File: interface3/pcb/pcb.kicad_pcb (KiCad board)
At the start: 4 copper layers, 55 x 50 mm, 26 parts, among them J1 Conn_Coaxial, T1 Murata 78602/8JC, U1 DS34LV86T, U2 DS34LV87T

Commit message: some pcb work
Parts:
- added U3: Pico_W, library:RPi_Pico_W_SMD_TH, F.Cu at (60.4, 86.4)
- moved C3 30.6 mm to (43.5, 105.7), turned to 0 degrees
- moved C1 28.6 mm to (43.5, 103.9), turned to 0 degrees
- moved C4 24.0 mm to (31.5, 105.7), turned to 0 degrees
- moved C2 21.5 mm to (31.5, 103.9), turned to 0 degrees
- moved U1 18.6 mm to (38.0, 99.2), turned to -90 degrees
- moved U2 16.7 mm to (26.0, 99.2), turned to -90 degrees
- moved H2 10.8 mm to (77.8, 111.9)
- moved H1 9.50 mm to (77.8, 63.8)
- moved R2 9.48 mm to (25.0, 92.8), turned to -90 degrees
- moved R1 7.23 mm to (27.0, 92.8), turned to 90 degrees
- moved R3 5.53 mm to (29.0, 92.8), turned to 90 degrees
- moved R8 5.21 mm to (37.0, 106.3)
- moved H3 5.14 mm to (20.2, 111.9)
- moved R11 5.12 mm to (37.0, 108.2)
- moved R12 5.12 mm to (37.0, 110.2)
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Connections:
- R11 pad 1: LED_TX -> ~{TX}
- R12 pad 1: LED_RX -> RX
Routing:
- net GND: track 26.2 -> 0.00 mm, vias 20 -> 0
- net RX+: track 17.2 -> 0.00 mm
- net TX-: track 19.1 -> 7.84 mm, vias 2 -> 0
- net Net-(U2A-OUT-): track 6.44 -> 0.00 mm
- net TX+: track 15.4 -> 9.24 mm
- net Net-(U2A-OUT+): track 6.08 -> 0.00 mm
- net Net-(U2B-OUT+): track 5.90 -> 0.00 mm
- net Net-(U2B-OUT-): track 5.55 -> 0.00 mm
- net Net-(D2-A): track 12.7 -> 8.33 mm
- net Net-(D3-A): track 10.0 -> 6.11 mm
- net +3V3: track 20.1 -> 16.3 mm, vias 4 -> 0
- net Net-(D1-A): track 15.0 -> 11.6 mm
- net RX-: track 3.23 -> 0.00 mm
- net Net-(D4-A): track 6.23 -> 4.49 mm
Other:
- board size 55 x 50 mm -> 65 x 55 mm

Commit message: pcb work
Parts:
- removed R16: 560, Resistor_SMD:R_0603_1608Metric
- added D5: STS, LED_SMD:LED_0603_1608Metric_Pad1.05x0.95mm_HandSolder, F.Cu at (185.5, 112.8)
- added D6: ERR, LED_SMD:LED_0603_1608Metric_Pad1.05x0.95mm_HandSolder, F.Cu at (185.5, 110.3)
- added R10: 560, Resistor_SMD:R_0603_1608Metric_Pad0.98x0.95mm_HandSolder, F.Cu at (181.0, 99.7)
- added R7: 560, Resistor_SMD:R_0603_1608Metric_Pad0.98x0.95mm_HandSolder, F.Cu at (181.0, 91.0)
- added R9: 560, Resistor_SMD:R_0603_1608Metric_Pad0.98x0.95mm_HandSolder, F.Cu at (181.0, 88.0)
- added SW1: Pico Run, Button_Switch_SMD:SW_Push_1P1T_NO_6x6mm_H9.5mm, F.Cu at (136.6, 126.6)
- C1, C2: value 0.1uF -> 0.1µ
- C3, C4: value 0.01uF -> 0.01µ
- D1: value GRN -> PWR; footprint LED_SMD:LED_0603_1608Metric -> LED_SMD:LED_0603_1608Metric_Pad1.05x0.95mm_HandSolder
- D2: value YEL -> TX; footprint LED_SMD:LED_0603_1608Metric -> LED_SMD:LED_0603_1608Metric_Pad1.05x0.95mm_HandSolder
- D3: value YEL -> RX; footprint LED_SMD:LED_0603_1608Metric -> LED_SMD:LED_0603_1608Metric_Pad1.05x0.95mm_HandSolder
- D4: value RED -> NET; footprint LED_SMD:LED_0603_1608Metric -> LED_SMD:LED_0603_1608Metric_Pad1.05x0.95mm_HandSolder
- R11, R12, R8: footprint Resistor_SMD:R_0603_1608Metric -> Resistor_SMD:R_0603_1608Metric_Pad0.98x0.95mm_HandSolder
- T1: value Murata 78602/8JC -> 78602/8JC
- moved D1 160.0 mm to (185.5, 122.8), turned to 180 degrees
- moved D2 157.3 mm to (185.5, 120.3), turned to 180 degrees
- moved D3 154.7 mm to (185.5, 117.8), turned to 180 degrees
- moved D4 152.1 mm to (185.5, 115.3), turned to 180 degrees
- moved R12 144.9 mm to (181.0, 93.9), turned to 0 degrees
- moved R11 144.4 mm to (181.0, 96.8), turned to 0 degrees
- moved R8 144.0 mm to (181.0, 102.7), turned to 0 degrees
- moved R2 118.7 mm to (143.2, 103.2), turned to 90 degrees
- moved R1 114.7 mm to (141.2, 103.1), turned to -90 degrees
- moved C2 114.0 mm to (144.9, 115.8)
- moved C4 114.0 mm to (144.9, 117.6)
- moved U2 114.0 mm to (139.4, 111.1)
- moved R5 111.7 mm to (141.3, 98.9)
- moved R3 110.8 mm to (139.2, 103.2), turned to -90 degrees
- moved H1 108.1 mm to (184.4, 81.3)
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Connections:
- R11 pad 1: ~{TX} -> LED_RX
- R11 pad 2: Net-(D2-A) -> Net-(D3-A)
- R12 pad 1: RX -> LED_NET
- R12 pad 2: Net-(D3-A) -> Net-(D4-A)
- R8 pad 1: LED_STATUS -> +3V3
- U3 pad 10: LED_ERROR -> unconnected-(U3-GPIO7-Pad10)
- U3 pad 11: LED_STATUS -> unconnected-(U3-GPIO8-Pad11)
- U3 pad 26: unconnected-(U3-GPIO20-Pad26) -> LED_TX
- U3 pad 27: unconnected-(U3-GPIO21-Pad27) -> LED_RX
- U3 pad 29: unconnected-(U3-GPIO22-Pad29) -> LED_NET
- U3 pad 30: unconnected-(U3-RUN-Pad30) -> PICO_RUN
- U3 pad 31: unconnected-(U3-GPIO26_ADC0-Pad31) -> LED_STS
- U3 pad 32: unconnected-(U3-GPIO27_ADC1-Pad32) -> LED_ERR
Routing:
- net +3V3: track 16.3 -> 127.7 mm, vias 0 -> 2
- net RX: track 0.00 -> 69.1 mm
- net PICO_RUN: track 0.00 -> 50.8 mm
- net ~{TX}: track 0.00 -> 37.8 mm
- net TX_ACTIVE: track 0.00 -> 28.6 mm
- net Net-(J1-Ext): track 13.3 -> 40.9 mm
- net Net-(D6-A): track 0.00 -> 27.4 mm
- net Net-(D5-A): track 0.00 -> 27.0 mm
- net TX-: track 7.84 -> 33.1 mm
- net LED_TX: track 0.00 -> 22.9 mm
- net Net-(D4-A): track 4.49 -> 27.2 mm
- net TX_DELAY: track 0.00 -> 22.5 mm
- net LED_RX: track 0.00 -> 21.2 mm
- net Net-(D3-A): track 6.11 -> 26.7 mm
- net LED_NET: track 0.00 -> 18.6 mm
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- added copper zone on F.Cu, net GND
- removed copper zone on In2.Cu, net +3V3
- removed copper zone on In1.Cu, net GND
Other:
- board size 65 x 55 mm -> 70.3 x 55 mm
- copper layers 4 -> 2
- board text removed: "COAX"
- board text removed: "ERR"
- board text removed: "PWR"
- board text removed: "RX"
- board text removed: "TX"

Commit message: interface3 pcb work
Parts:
- added D10: NET, LED_SMD:LED_0603_1608Metric, F.Cu at (184.9, 129.0)
- added D11: STS, LED_SMD:LED_0603_1608Metric, F.Cu at (188.2, 129.0)
- added D12: ERR, LED_SMD:LED_0603_1608Metric, F.Cu at (191.5, 129.0)
- added D7: RX3, LED_SMD:LED_0603_1608Metric, F.Cu at (175.0, 129.0)
- added D8: TX4, LED_SMD:LED_0603_1608Metric, F.Cu at (178.3, 129.0)
- added D9: RX4, LED_SMD:LED_0603_1608Metric, F.Cu at (181.6, 129.0)
- added J2: Conn_Coaxial, Connector_Coaxial:BNC_Amphenol_B6252HB-NPP3G-50_Horizontal, F.Cu at (121.1, 93.4)
- added J3: PMOD, Connector_PinHeader_2.54mm:PinHeader_2x06_P2.54mm_Vertical, F.Cu at (128.8, 83.0)
- added R13: 560, Resistor_SMD:R_0603_1608Metric_Pad0.98x0.95mm_HandSolder, F.Cu at (155.6, 143.2)
- added R14: 560, Resistor_SMD:R_0603_1608Metric_Pad0.98x0.95mm_HandSolder, F.Cu at (155.6, 145.7)
- added R15: 560, Resistor_SMD:R_0603_1608Metric_Pad0.98x0.95mm_HandSolder, F.Cu at (155.6, 148.2)
- added R16: 560, Resistor_SMD:R_0603_1608Metric_Pad0.98x0.95mm_HandSolder, F.Cu at (155.6, 150.7)
- added R17: 560, Resistor_SMD:R_0603_1608Metric_Pad0.98x0.95mm_HandSolder, F.Cu at (155.6, 153.3)
- added R18: 560, Resistor_SMD:R_0603_1608Metric_Pad0.98x0.95mm_HandSolder, F.Cu at (155.6, 155.8)
- added R19: 560, Resistor_SMD:R_0603_1608Metric_Pad0.98x0.95mm_HandSolder, F.Cu at (155.6, 158.3)
- added R20: 560, Resistor_SMD:R_0603_1608Metric_Pad0.98x0.95mm_HandSolder, F.Cu at (155.6, 160.8)
- added R21: 560, Resistor_SMD:R_0603_1608Metric_Pad0.98x0.95mm_HandSolder, F.Cu at (159.9, 143.2)
- added R22: 560, Resistor_SMD:R_0603_1608Metric_Pad0.98x0.95mm_HandSolder, F.Cu at (159.9, 145.7)
- added R23: 560, Resistor_SMD:R_0603_1608Metric_Pad0.98x0.95mm_HandSolder, F.Cu at (159.9, 148.2)
- added R24: 560, Resistor_SMD:R_0603_1608Metric_Pad0.98x0.95mm_HandSolder, F.Cu at (159.9, 150.7)
- added T2: 78602/8JC, library:Murata_786J, F.Cu at (133.5, 96.5)
- C1, C4: footprint Capacitor_SMD:C_0603_1608Metric -> Capacitor_SMD:C_0603_1608Metric_Pad1.08x0.95mm_HandSolder
- C2: value 0.1µ -> 0.01µ; footprint Capacitor_SMD:C_0603_1608Metric -> Capacitor_SMD:C_0603_1608Metric_Pad1.08x0.95mm_HandSolder
- C3: value 0.01µ -> 0.1µ; footprint Capacitor_SMD:C_0603_1608Metric -> Capacitor_SMD:C_0603_1608Metric_Pad1.08x0.95mm_HandSolder
- D1: footprint LED_SMD:LED_0603_1608Metric_Pad1.05x0.95mm_HandSolder -> LED_SMD:LED_0603_1608Metric
- D2: value TX -> TX1; footprint LED_SMD:LED_0603_1608Metric_Pad1.05x0.95mm_HandSolder -> LED_SMD:LED_0603_1608Metric
- D3: value RX -> RX1; footprint LED_SMD:LED_0603_1608Metric_Pad1.05x0.95mm_HandSolder -> LED_SMD:LED_0603_1608Metric
- D4: value NET -> TX2; footprint LED_SMD:LED_0603_1608Metric_Pad1.05x0.95mm_HandSolder -> LED_SMD:LED_0603_1608Metric
- D5: value STS -> RX2; footprint LED_SMD:LED_0603_1608Metric_Pad1.05x0.95mm_HandSolder -> LED_SMD:LED_0603_1608Metric
- D6: value ERR -> TX3; footprint LED_SMD:LED_0603_1608Metric_Pad1.05x0.95mm_HandSolder -> LED_SMD:LED_0603_1608Metric
- R1: value 150 -> 120; footprint Resistor_SMD:R_0603_1608Metric -> Resistor_SMD:R_0603_1608Metric_Pad0.98x0.95mm_HandSolder
- R10: value 560 -> 510
- R11, R12: value 560 -> 33
- R2: footprint Resistor_SMD:R_0603_1608Metric -> Resistor_SMD:R_0603_1608Metric_Pad0.98x0.95mm_HandSolder
- R3: value 33 -> 150; footprint Resistor_SMD:R_0603_1608Metric -> Resistor_SMD:R_0603_1608Metric_Pad0.98x0.95mm_HandSolder
- R4: value 33 -> 510; footprint Resistor_SMD:R_0603_1608Metric -> Resistor_SMD:R_0603_1608Metric_Pad0.98x0.95mm_HandSolder
- R5: value 510 -> 33; footprint Resistor_SMD:R_0603_1608Metric -> Resistor_SMD:R_0603_1608Metric_Pad0.98x0.95mm_HandSolder
- R6: value 120 -> 33; footprint Resistor_SMD:R_0603_1608Metric -> Resistor_SMD:R_0603_1608Metric_Pad0.98x0.95mm_HandSolder
- R7: value 560 -> 120
- R8, R9: value 560 -> 150
- moved H3 90.1 mm to (198.5, 82.0)
- moved H4 89.8 mm to (198.0, 129.0)
- moved H1 72.4 mm to (112.0, 82.0)
- moved H2 72.4 mm to (112.0, 129.0)
- moved SW1 57.6 mm to (193.8, 119.1)
- moved R7 46.7 mm to (134.4, 89.2)
- moved R8 44.3 mm to (136.7, 102.4)
- moved R9 39.1 mm to (142.0, 90.4)
- moved R11 38.9 mm to (142.5, 102.4)
- moved R12 38.6 mm to (142.7, 99.3)
- moved R10 38.6 mm to (142.7, 94.7)
- moved R6 33.1 mm to (144.0, 125.0), turned to 0 degrees
- moved D1 31.0 mm to (155.2, 129.0), turned to 0 degrees
- moved U1 28.8 mm to (155.0, 104.5), turned to 0 degrees
- moved J1 28.6 mm to (121.1, 116.6), turned to 90 degrees
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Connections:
- net RX renamed RX1
- net RX+ renamed RX1+
- net RX- renamed RX1-
- net TX_ACTIVE renamed TX1_ACTIVE
- net TX_DELAY renamed TX1_DELAY
- net ~{TX} renamed ~{TX1}
- R1 pad 1: TX+ -> Net-(J1-In)
- R1 pad 2: Net-(U2A-OUT-) -> Net-(J1-Ext)
- R10 pad 1: LED_TX -> TX2-
- R10 pad 2: Net-(D2-A) -> TX2+
- R11 pad 1: LED_RX -> TX2+
- R11 pad 2: Net-(D3-A) -> Net-(U2D-OUT-)
- R12 pad 1: LED_NET -> TX2-
- R12 pad 2: Net-(D4-A) -> Net-(U2D-OUT+)
- R2 pad 1: Net-(U2A-OUT+) -> TX1+
- R2 pad 2: TX- -> Net-(U2A-OUT-)
- R3 pad 1: TX+ -> Net-(U2A-OUT+)
- R3 pad 2: Net-(U2B-OUT-) -> TX1-
- R4 pad 1: TX- -> TX1-
- R4 pad 2: Net-(U2B-OUT+) -> TX1+
- R5 pad 1: TX- -> TX1+
- R5 pad 2: TX+ -> Net-(U2B-OUT-)
- R6 pad 1: Net-(J1-In) -> TX1-
- R6 pad 2: Net-(J1-Ext) -> Net-(U2B-OUT+)
- R7 pad 1: LED_STS -> Net-(J2-In)
- R7 pad 2: Net-(D5-A) -> Net-(J2-Ext)
- R8 pad 1: +3V3 -> TX2+
- R8 pad 2: Net-(D1-A) -> Net-(U2C-OUT-)
- R9 pad 1: LED_ERR -> Net-(U2C-OUT+)
- R9 pad 2: Net-(D6-A) -> TX2-
- T1 pad 3: TX+ -> TX1+
- T1 pad 4: TX- -> TX1-
- U1 pad 1: GND -> RX2-
- U1 pad 2: GND -> RX2+
- U1 pad 3: unconnected-(U1A-OUT-Pad3) -> RX2
- U2 pad 10: unconnected-(U2C-OUT+-Pad10) -> Net-(U2C-OUT+)
- U2 pad 11: unconnected-(U2C-OUT--Pad11) -> Net-(U2C-OUT-)
- U2 pad 12: GND -> TX2_ACTIVE
- U2 pad 13: unconnected-(U2D-OUT--Pad13) -> Net-(U2D-OUT-)
- U2 pad 14: unconnected-(U2D-OUT+-Pad14) -> Net-(U2D-OUT+)
- U2 pad 15: GND -> ~{TX2}
- U2 pad 9: GND -> TX2_DELAY
- U3 pad 10: unconnected-(U3-GPIO7-Pad10) -> LED_RX1
- U3 pad 11: unconnected-(U3-GPIO8-Pad11) -> LED_TX1
- U3 pad 12: unconnected-(U3-GPIO9-Pad12) -> RX2
- U3 pad 13: unconnected-(U3-GND-Pad13) -> ~{TX2}
- U3 pad 14: unconnected-(U3-GPIO10-Pad14) -> TX2_ACTIVE
- U3 pad 15: unconnected-(U3-GPIO11-Pad15) -> TX2_DELAY
- U3 pad 16: unconnected-(U3-GPIO12-Pad16) -> LED_RX2
- U3 pad 17: unconnected-(U3-GPIO13-Pad17) -> LED_TX2
- U3 pad 19: unconnected-(U3-GPIO14-Pad19) -> RX3
- U3 pad 20: unconnected-(U3-GPIO15-Pad20) -> TX3
- U3 pad 21: unconnected-(U3-GPIO16-Pad21) -> TX3_ACTIVE
- U3 pad 22: unconnected-(U3-GPIO17-Pad22) -> TX3_DELAY
- U3 pad 24: unconnected-(U3-GPIO18-Pad24) -> RX4
- U3 pad 25: unconnected-(U3-GPIO19-Pad25) -> TX4
- U3 pad 26: LED_TX -> TX4_ACTIVE
- U3 pad 27: LED_RX -> TX4_DELAY
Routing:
- net +3V3: track 127.7 -> 0.00 mm, vias 2 -> 0
- net RX1: track 69.1 -> 0.00 mm
- net PICO_RUN: track 50.8 -> 0.00 mm
- net Net-(J1-Ext): track 40.9 -> 0.00 mm, vias 1 -> 0
- net ~{TX1}: track 37.8 -> 0.00 mm
- net TX-: track 33.1 -> 0.00 mm
- net TX1_ACTIVE: track 28.6 -> 0.00 mm
- net Net-(D6-A): track 27.4 -> 0.00 mm
- net Net-(D4-A): track 27.2 -> 0.00 mm
- net Net-(D5-A): track 27.0 -> 0.00 mm
- net Net-(D3-A): track 26.7 -> 0.00 mm
- net Net-(D2-A): track 26.6 -> 0.00 mm
- net Net-(D1-A): track 26.0 -> 0.00 mm
- net LED_TX: track 22.9 -> 0.00 mm
- net TX1_DELAY: track 22.5 -> 0.00 mm
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- removed copper zone on B.Cu, net GND
- removed copper zone on F.Cu, net GND
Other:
- board size 70.3 x 55 mm -> 107.4 x 79.4 mm

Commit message: interface3 version 1 pcb sent to jlcpcb
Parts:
- added J4: POWER, Connector_USB:USB_B_OST_USB-B1HSxx_Horizontal, F.Cu at (123.8, 118.8)
- J1: value Conn_Coaxial -> PORT1
- J2: value Conn_Coaxial -> PORT2
- J3: value PMOD -> PORT3/4
- moved J3 63.9 mm to (191.9, 72.5)
- moved R24 52.2 mm to (205.5, 125.2), turned to -90 degrees
- moved R20 51.1 mm to (192.3, 125.2), turned to -90 degrees
- moved R23 48.1 mm to (202.2, 125.2), turned to -90 degrees
- moved R19 47.0 mm to (189.0, 125.2), turned to -90 degrees
- moved R22 44.0 mm to (198.9, 125.2), turned to -90 degrees
- moved R18 42.9 mm to (185.6, 125.2), turned to -90 degrees
- moved R21 39.9 mm to (195.6, 125.2), turned to -90 degrees
- moved R17 38.8 mm to (182.3, 125.2), turned to -90 degrees
- moved SW1 38.2 mm to (156.5, 127.0)
- moved R16 34.7 mm to (179.0, 125.2), turned to -90 degrees
- moved R15 30.6 mm to (175.7, 125.2), turned to -90 degrees
- moved R6 27.9 mm to (143.9, 97.1)
- moved R14 26.6 mm to (172.4, 125.2), turned to -90 degrees
- moved R5 23.2 mm to (143.9, 103.2)
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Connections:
- U3 pad 1: unconnected-(U3-GPIO0-Pad1) -> LED_RX3
- U3 pad 2: unconnected-(U3-GPIO1-Pad2) -> LED_TX3
- U3 pad 34: unconnected-(U3-GPIO28_ADC2-Pad34) -> LED_TX4
- U3 pad 40: unconnected-(U3-VBUS-Pad40) -> VBUS
- U3 pad 9: unconnected-(U3-GPIO6-Pad9) -> LED_RX4
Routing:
- net +3V3: track 0.00 -> 151.5 mm, vias 0 -> 8
- net VBUS: track 0.00 -> 102.1 mm, vias 0 -> 2
- net PICO_RUN: track 0.00 -> 72.5 mm, vias 0 -> 3
- net ~{TX2}: track 0.00 -> 63.3 mm, vias 0 -> 5
- net TX2_DELAY: track 0.00 -> 62.2 mm, vias 0 -> 3
- net TX2_ACTIVE: track 0.00 -> 61.6 mm, vias 0 -> 3
- net TX1_DELAY: track 0.00 -> 54.6 mm, vias 0 -> 3
- net LED_ERR: track 0.00 -> 53.4 mm, vias 0 -> 3
- net RX3: track 0.00 -> 48.2 mm, vias 0 -> 1
- net LED_STS: track 0.00 -> 48.2 mm, vias 0 -> 3
- net TX1_ACTIVE: track 0.00 -> 47.8 mm, vias 0 -> 2
- net TX3: track 0.00 -> 47.7 mm, vias 0 -> 1
- net LED_TX4: track 0.00 -> 47.7 mm, vias 0 -> 3
- net RX2: track 0.00 -> 47.0 mm, vias 0 -> 1
- net LED_TX2: track 0.00 -> 42.2 mm, vias 0 -> 3
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- added copper zone on F.Cu, net GND
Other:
- board size 107.4 x 79.4 mm -> 107.5 x 66 mm
- board text added: "+3V3"
- board text added: "3"
- board text added: "4"
- board text added: "GND"
- board text added: "IBM 3270 Interface https://github.com/lowobservable/coax interface3 - Rev 1 - Hans Hübner"
- board text added: "RX"
- board text added: "TX"
- board text added: "TX_ACTIVE"
- board text added: "TX_DELAY"
- board text removed: "IBM 3270 Interface https://ajk.me/v2xp interface3 - Rev 1"

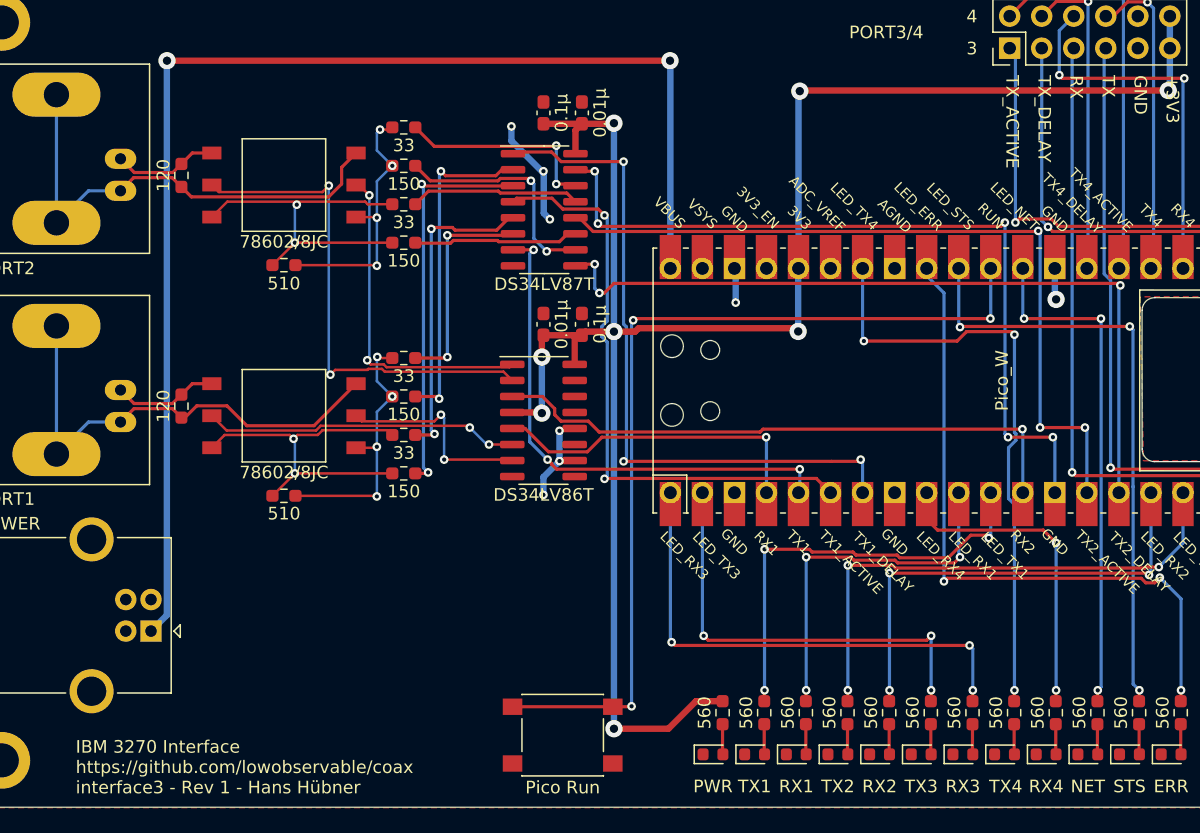
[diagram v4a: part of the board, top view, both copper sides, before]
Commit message: fix PCB issues found in v1
closes #1, #2, #3
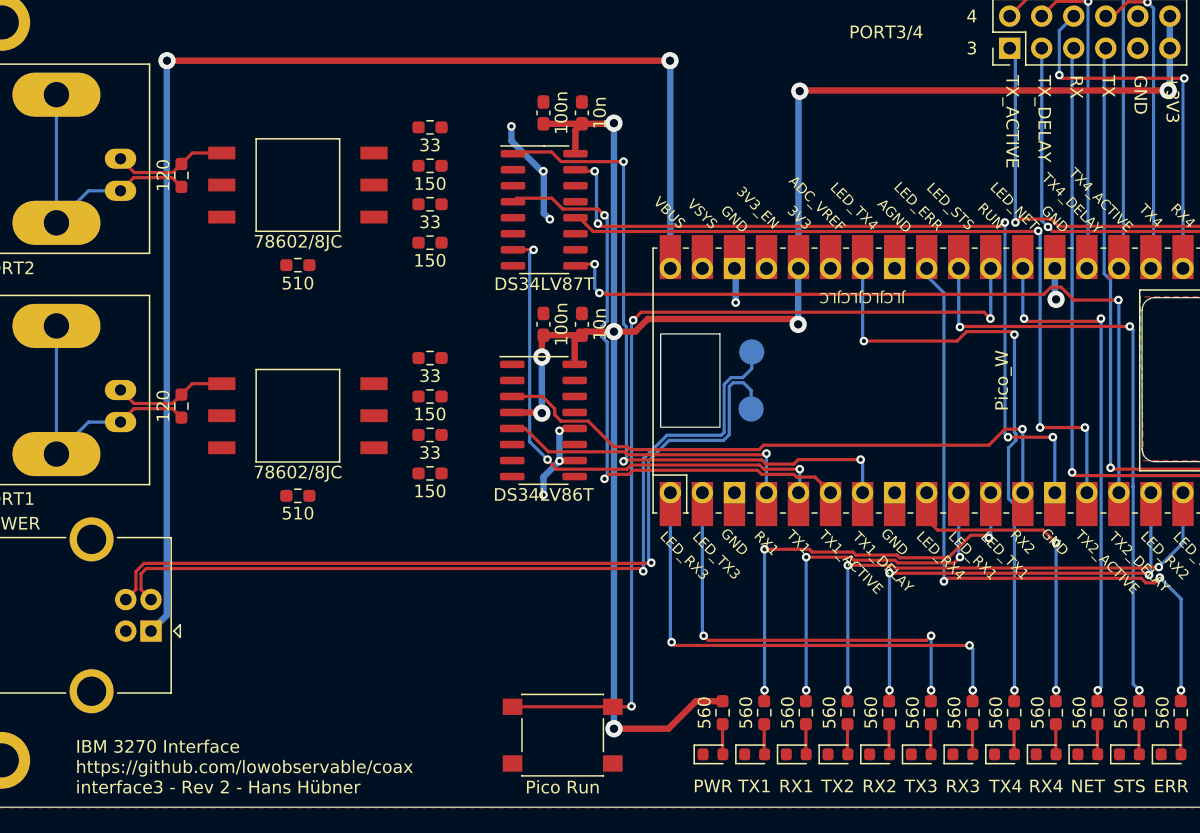
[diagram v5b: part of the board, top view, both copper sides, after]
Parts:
- added TP2: D-, TestPoint:TestPoint_Pad_D2.0mm, B.Cu at (171.4, 96.6)
- added TP3: D+, TestPoint:TestPoint_Pad_D2.0mm, B.Cu at (171.4, 101.1)
- C1: value 0.1µ -> 100n
- C2: value 0.01µ -> 10n
- C3: value 0.1µ -> 10n
- C4: value 0.01µ -> 100n
- moved R11 2.08 mm to (145.9, 84.9)
- moved R12 2.08 mm to (145.9, 78.8)
- moved R2 2.08 mm to (145.9, 106.2)
- moved R3 2.08 mm to (145.9, 100.2)
- moved R5 2.08 mm to (145.9, 103.2)
- moved R6 2.08 mm to (145.9, 97.1)
- moved R8 2.08 mm to (145.9, 88.0)
- moved R9 2.08 mm to (145.9, 81.9)
- moved R10 1.10 mm to (135.5, 89.7)
- moved R4 1.10 mm to (135.5, 108.0)
- moved T1 1.10 mm to (135.5, 101.7)
- moved T2 1.10 mm to (135.5, 83.4)
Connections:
- J4 pad 2: unconnected-(J4-D--Pad2) -> Net-(J4-D-)
- J4 pad 3: unconnected-(J4-D+-Pad3) -> Net-(J4-D+)
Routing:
- net Net-(J4-D+): track 0.00 -> 66.5 mm, vias 0 -> 1
- net Net-(J4-D-): track 0.00 -> 66.5 mm, vias 0 -> 1
- net RX2+: track 39.7 -> 0.00 mm, vias 2 -> 0
- net Net-(U2A-OUT-): track 31.4 -> 0.00 mm, vias 2 -> 0
- net TX1+: track 28.3 -> 0.00 mm, vias 2 -> 0
- net TX2+: track 28.2 -> 0.00 mm, vias 2 -> 0
- net RX2-: track 26.4 -> 0.00 mm, vias 2 -> 0
- net Net-(U2A-OUT+): track 26.1 -> 0.00 mm, vias 2 -> 0
- net RX1+: track 25.1 -> 0.00 mm, vias 2 -> 0
- net Net-(U2B-OUT-): track 24.9 -> 0.00 mm, vias 2 -> 0
- net TX1-: track 21.5 -> 0.00 mm, vias 4 -> 0
- net TX2-: track 21.1 -> 0.00 mm, vias 4 -> 0
- net Net-(U2C-OUT+): track 18.3 -> 0.00 mm, vias 2 -> 0
- net Net-(U2B-OUT+): track 17.5 -> 0.00 mm, vias 2 -> 0
- net Net-(U2D-OUT+): track 16.4 -> 0.00 mm, vias 2 -> 0
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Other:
- board text added: "IBM 3270 Interface https://github.com/lowobservable/coax interface3 - Rev 2 - Hans Hübner"
- board text removed: "IBM 3270 Interface https://github.com/lowobservable/coax interface3 - Rev 1 - Hans Hübner"

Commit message: finish layout (again) - this version has not been produced yet
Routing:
- net RX2+: track 0.00 -> 40.3 mm, vias 0 -> 2
- net Net-(U2A-OUT-): track 0.00 -> 28.4 mm, vias 0 -> 2
- net RX2-: track 0.00 -> 26.3 mm, vias 0 -> 2
- net TX2+: track 0.00 -> 24.8 mm, vias 0 -> 3
- net RX1+: track 0.00 -> 24.6 mm
- net Net-(U2A-OUT+): track 0.00 -> 24.2 mm, vias 0 -> 2
- net Net-(U2B-OUT-): track 0.00 -> 23.1 mm, vias 0 -> 2
- net TX2-: track 0.00 -> 18.8 mm, vias 0 -> 3
- net TX1+: track 0.00 -> 18.5 mm
- net Net-(U2C-OUT+): track 0.00 -> 17.3 mm, vias 0 -> 2
- net Net-(J2-Ext): track 21.9 -> 38.7 mm
- net Net-(J1-Ext): track 21.9 -> 38.2 mm
- net RX1-: track 0.00 -> 15.7 mm
- net Net-(U2B-OUT+): track 0.00 -> 15.7 mm, vias 0 -> 2
- net Net-(U2D-OUT+): track 0.00 -> 14.7 mm, vias 0 -> 2
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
